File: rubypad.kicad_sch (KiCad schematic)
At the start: 1 part

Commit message: save changes
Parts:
- removed U?: Elite-C, symbol keebio:Elite-C
- added D1, D2, D3, D4, D5, D6: D_Small, Keebio-Parts:Diode-dual, symbol Device:D_Small
- added MX1, MX2, MX3, MX4, MX5, MX6: MX-NoLED, MX_Only:MXOnly-1U-Hotswap-Antishear, symbol MX_Alps_Hybrid:MX-NoLED
- added U1: ProMicro, Keebio-Parts:ArduinoProMicro, symbol keebio:ProMicro
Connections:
- new net: D6.2 (A), MX6.2 (ROW)
- new net: D1.2 (A), MX1.2 (ROW)
- new net: D5.2 (A), MX5.2 (ROW)
- new net: D3.2 (A), MX3.2 (ROW)
- new net: D4.2 (A), MX4.2 (ROW)
- new net: D2.2 (A), MX2.2 (ROW)
- new net col0: MX1.1 (COL), MX4.1 (COL)
- new net col1: MX2.1 (COL), MX5.1 (COL)
- new net col2: MX3.1 (COL), MX6.1 (COL)
- new net row0: D1.1 (K), D2.1 (K), D3.1 (K)
- new net row1: D4.1 (K), D5.1 (K), D6.1 (K)

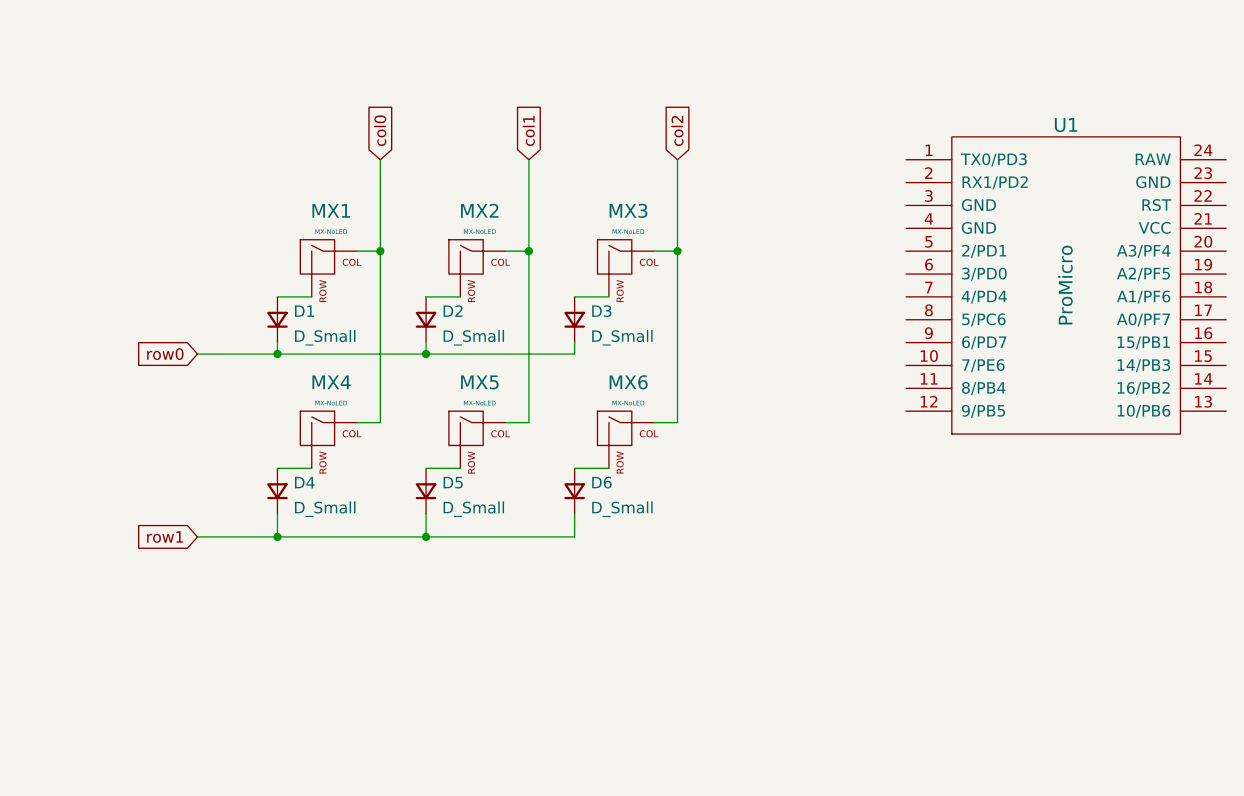
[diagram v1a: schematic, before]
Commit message: Setup encoder schematic
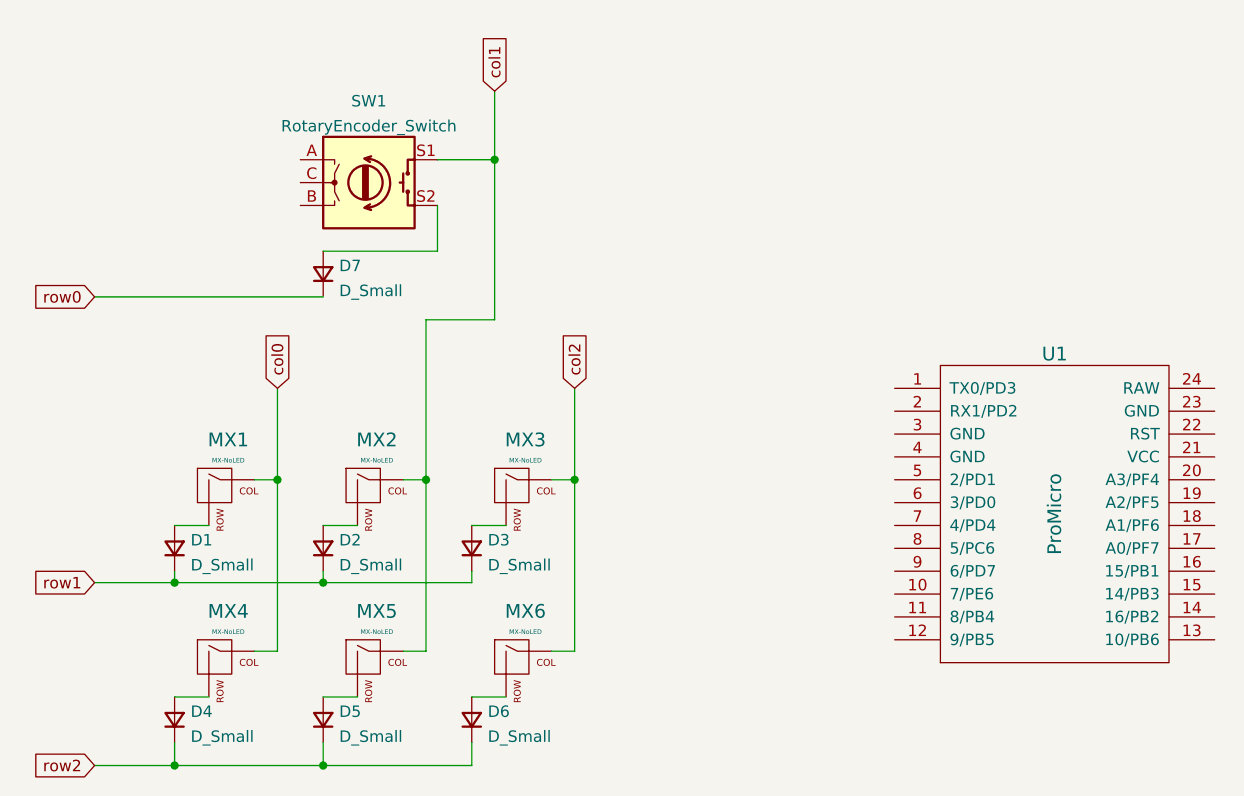
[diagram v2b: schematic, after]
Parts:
- added D7: D_Small, Keebio-Parts:Diode-dual, symbol Device:D_Small
- added SW1: RotaryEncoder_Switch, Keebio-Parts:RotaryEncoder_EC11, symbol Device:RotaryEncoder_Switch
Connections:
- net col1: now also SW1.S1
- net row0: now also D7.1 (K); no longer D1.1 (K), D2.1 (K), D3.1 (K)
- net row1: now also D1.1 (K), D2.1 (K), D3.1 (K); no longer D4.1 (K), D5.1 (K), D6.1 (K)
- new net: D7.2 (A), SW1.S2
- new net row2: D4.1 (K), D5.1 (K), D6.1 (K)
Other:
- moved on the sheet: D1, D2, D3, D4, D5, D6, MX1, MX2, MX3, MX4, MX5, MX6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

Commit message: Update - ran traces
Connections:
- net col0: now also U1.7 (4/PD4)
- net col1: now also U1.8 (5/PC6)
- net col2: now also U1.9 (6/PD7)
- net row0: now also U1.10 (7/PE6)
- net row1: now also U1.12 (9/PB5)
- net row2: now also U1.11 (8/PB4)
- net ENCB: now reaches U1.13 (10/PB6)
- net ENCB: now also SW1.B
- net ENCC: now reaches U1.14 (16/PB2)
- net ENCC: now also SW1.C
- net ENCA: now reaches U1.15 (14/PB3)
- net ENCA: now also SW1.A
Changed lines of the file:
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@@
+    (stroke (width 0) (type default) (color 0 0 0 0))
+  )
+  (wire (pts (xy 165.1 80.01) (xy 179.07 80.01))
     (stroke (width 0) (type default) (color 0 0 0 0))
   )
@@
     (stroke (width 0) (type default) (color 0 0 0 0))
   )
+  (wire (pts (xy 55.88 31.75) (xy 63.5 31.75))
+    (stroke (width 0) (type default) (color 0 0 0 0))
+  )
   (wire (pts (xy 85.09 29.21) (xy 85.09 46.99))
     (stroke (width 0) (type default) (color 0 0 0 0))
@@
     (stroke (width 0) (type default) (color 0 0 0 0))
   )
+  (wire (pts (xy 119.38 80.01) (xy 129.54 80.01))
+    (stroke (width 0) (type default) (color 0 0 0 0))
+  )
+  (wire (pts (xy 165.1 82.55) (xy 171.45 82.55))
+    (stroke (width 0) (type default) (color 0 0 0 0))
+  )
   (wire (pts (xy 74.93 64.77) (xy 77.47 64.77))
     (stroke (width 0) (type default) (color 0 0 0 0))
   )
+  (wire (pts (xy 123.19 82.55) (xy 129.54 82.55))
+    (stroke (width 0) (type default) (color 0 0 0 0))
+  )
   (wire (pts (xy 66.04 88.9) (xy 69.85 88.9))
     (stroke (width 0) (type default) (color 0 0 0 0))
@@
     )
   )
+  (global_label "ENCB" (shape input) (at 63.5 34.29 180) (fields_autoplaced)
+    (effects (font (size 1.27 1.27)) (justify right))
+    (property "Intersheet References" "${INTERSHEET_REFS}" (id 0) (at 56.0674 34.2106 0)
+      (effects (font (size 1.27 1.27)) (justify right) hide)
+    )
+  )
+  (global_label "ENCC" (shape input) (at 179.07 80.01 0) (fields_autoplaced)
+    (effects (font (size 1.27 1.27)) (justify left))
+    (property "Intersheet References" "${INTERSHEET_REFS}" (id 0) (at 186.5026 80.0894 0)
+      (effects (font (size 1.27 1.27)) (justify left) hide)
+    )
+  )
+  (global_label "col2" (shape input) (at 129.54 74.93 180) (fields_autoplaced)
+    (effects (font (size 1.27 1.27)) (justify right))
+    (property "Intersheet References" "${INTERSHEET_REFS}" (id 0) (at 123.0145 75.0094 0)
+      (effects (font (size 1.27 1.27)) (justify right) hide)
+    )
+  )
   (global_label "row1" (shape input) (at 40.64 76.2 180) (fields_autoplaced)
     (effects (font (size 1.27 1.27)) (justify right))
@@
     )
   )
+  (global_label "row2" (shape input) (at 119.38 80.01 180) (fields_autoplaced)
+    (effects (font (size 1.27 1.27)) (justify right))
+    (property "Intersheet References" "${INTERSHEET_REFS}" (id 0) (at 112.4917 79.9306 0)
+      (effects (font (size 1.27 1.27)) (justify right) hide)
+    )
+  )
   (global_label "col2" (shape input) (at 93.98 54.61 90) (fields_autoplaced)
     (effects (font (size 1.27 1.27)) (justify left))
@@
     )
   )
+  (global_label "col0" (shape input) (at 129.54 69.85 180) (fields_autoplaced)
+    (effects (font (size 1.27 1.27)) (justify right))
+    (property "Intersheet References" "${INTERSHEET_REFS}" (id 0) (at 123.0145 69.9294 0)
+      (effects (font (size 1.27 1.27)) (justify right) hide)
+    )
+  )
   (global_label "col1" (shape input) (at 85.09 21.59 90) (fields_autoplaced)
     (effects (font (size 1.27 1.27)) (justify left))
@@
     )
   )
+  (global_label "ENCC" (shape input) (at 55.88 31.75 180) (fields_autoplaced)
+    (effects (font (size 1.27 1.27)) (justify right))
+    (property "Intersheet References" "${INTERSHEET_REFS}" (id 0) (at 48.4474 31.6706 0)
+      (effects (font (size 1.27 1.27)) (justify right) hide)
+    )
+  )
+  (global_label "row0" (shape input) (at 129.54 77.47 180) (fields_autoplaced)
+    (effects (font (size 1.27 1.27)) (justify right))
+    (property "Intersheet References" "${INTERSHEET_REFS}" (id 0) (at 122.6517 77.3906 0)
+      (effects (font (size 1.27 1.27)) (justify right) hide)
+    )
+  )
+  (global_label "ENCA" (shape input) (at 165.1 77.47 0) (fields_autoplaced)
+    (effects (font (size 1.27 1.27)) (justify left))
+    (property "Intersheet References" "${INTERSHEET_REFS}" (id 0) (at 172.3512 77.5494 0)
+      (effects (font (size 1.27 1.27)) (justify left) hide)
+    )
+  )
+  (global_label "ENCA" (shape input) (at 63.5 29.21 180) (fields_autoplaced)
+    (effects (font (size 1.27 1.27)) (justify right))
+    (property "Intersheet References" "${INTERSHEET_REFS}" (id 0) (at 56.2488 29.1306 0)
+      (effects (font (size 1.27 1.27)) (justify right) hide)
+    )
+  )
+  (global_label "row1" (shape input) (at 123.19 82.55 180) (fields_autoplaced)
+    (effects (font (size 1.27 1.27)) (justify right))
+    (property "Intersheet References" "${INTERSHEET_REFS}" (id 0) (at 116.3017 82.4706 0)
+      (effects (font (size 1.27 1.27)) (justify right) hide)
+    )
+  )
   (global_label "col0" (shape input) (at 60.96 54.61 90) (fields_autoplaced)
     (effects (font (size 1.27 1.27)) (justify left))
@@
     )
   )
+  (global_label "col1" (shape input) (at 129.54 72.39 180) (fields_autoplaced)
+    (effects (font (size 1.27 1.27)) (justify right))
+    (property "Intersheet References" "${INTERSHEET_REFS}" (id 0) (at 123.0145 72.4694 0)
+      (effects (font (size 1.27 1.27)) (justify right) hide)
+    )
+  )
+  (global_label "ENCB" (shape input) (at 171.45 82.55 0) (fields_autoplaced)
+    (effects (font (size 1.27 1.27)) (justify left))
+    (property "Intersheet References" "${INTERSHEET_REFS}" (id 0) (at 178.8826 82.6294 0)
+      (effects (font (size 1.27 1.27)) (justify left) hide)
+    )
+  )

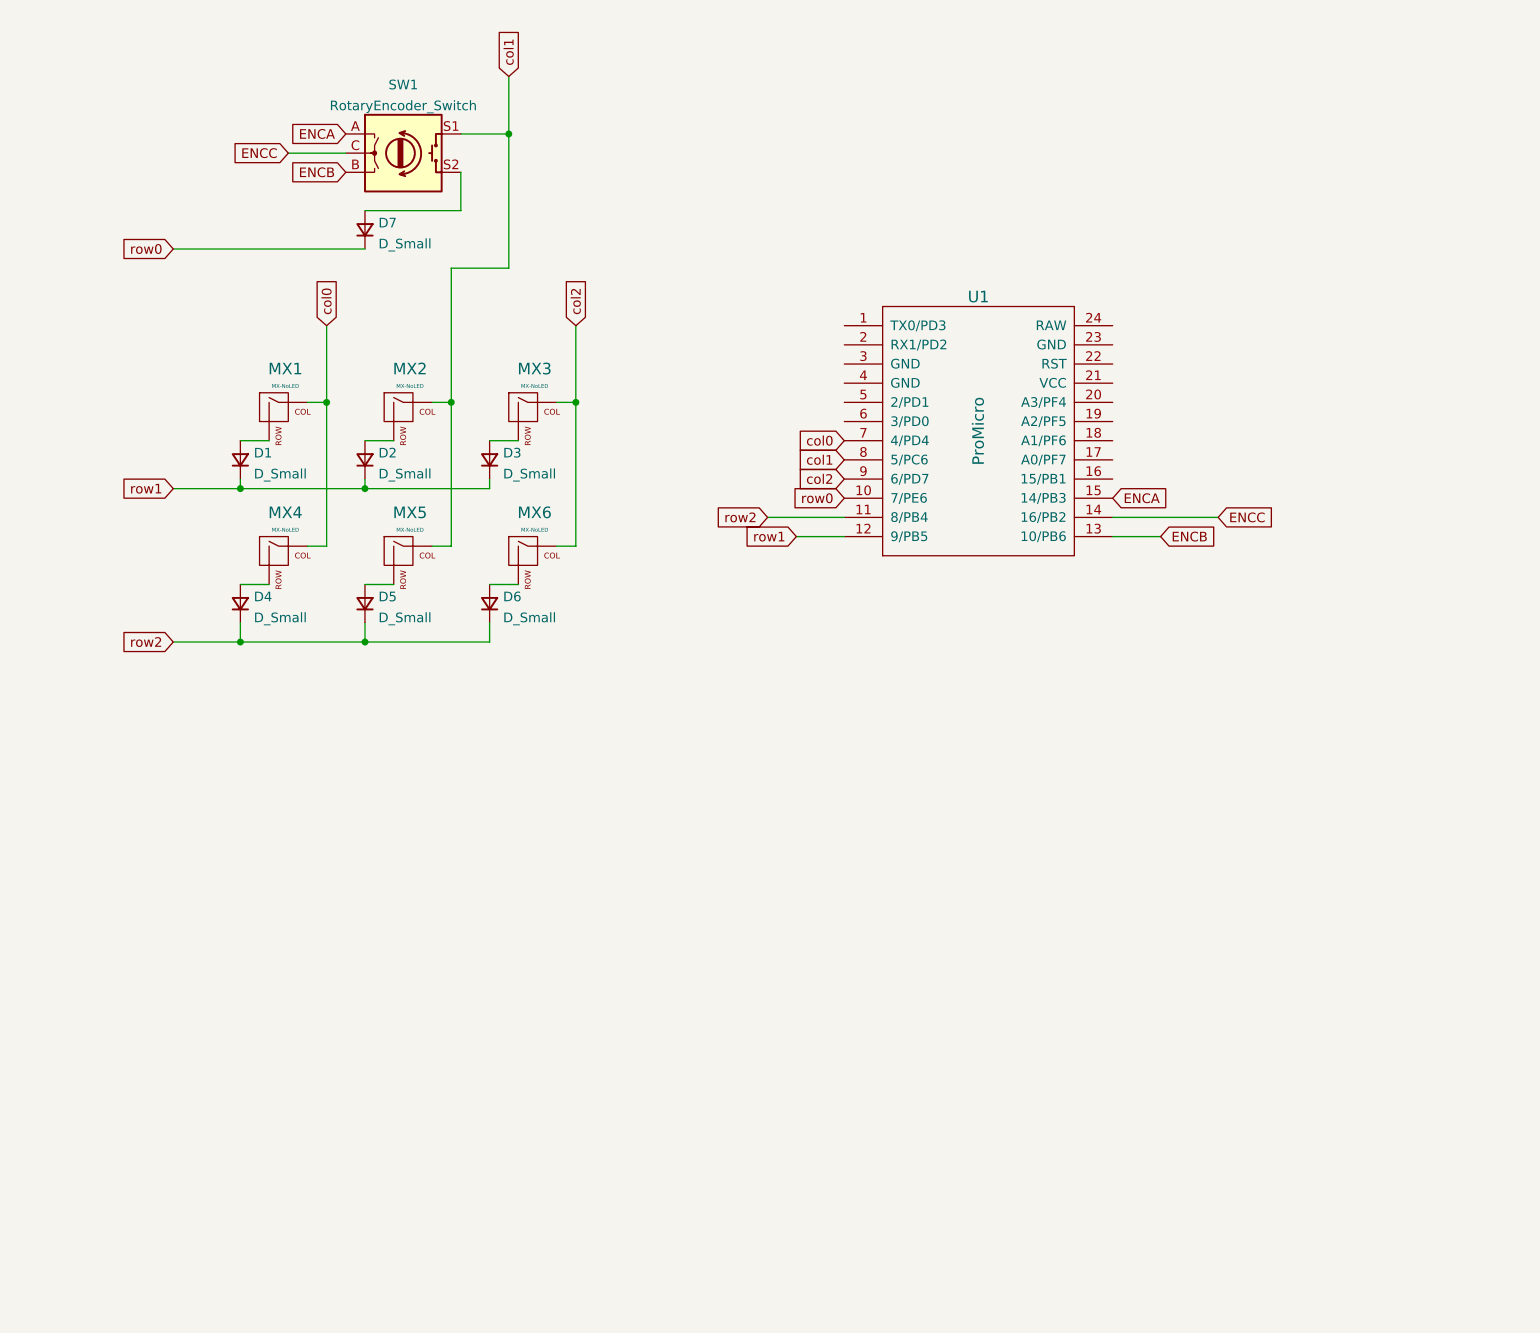
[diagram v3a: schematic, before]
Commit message: Added 3d models
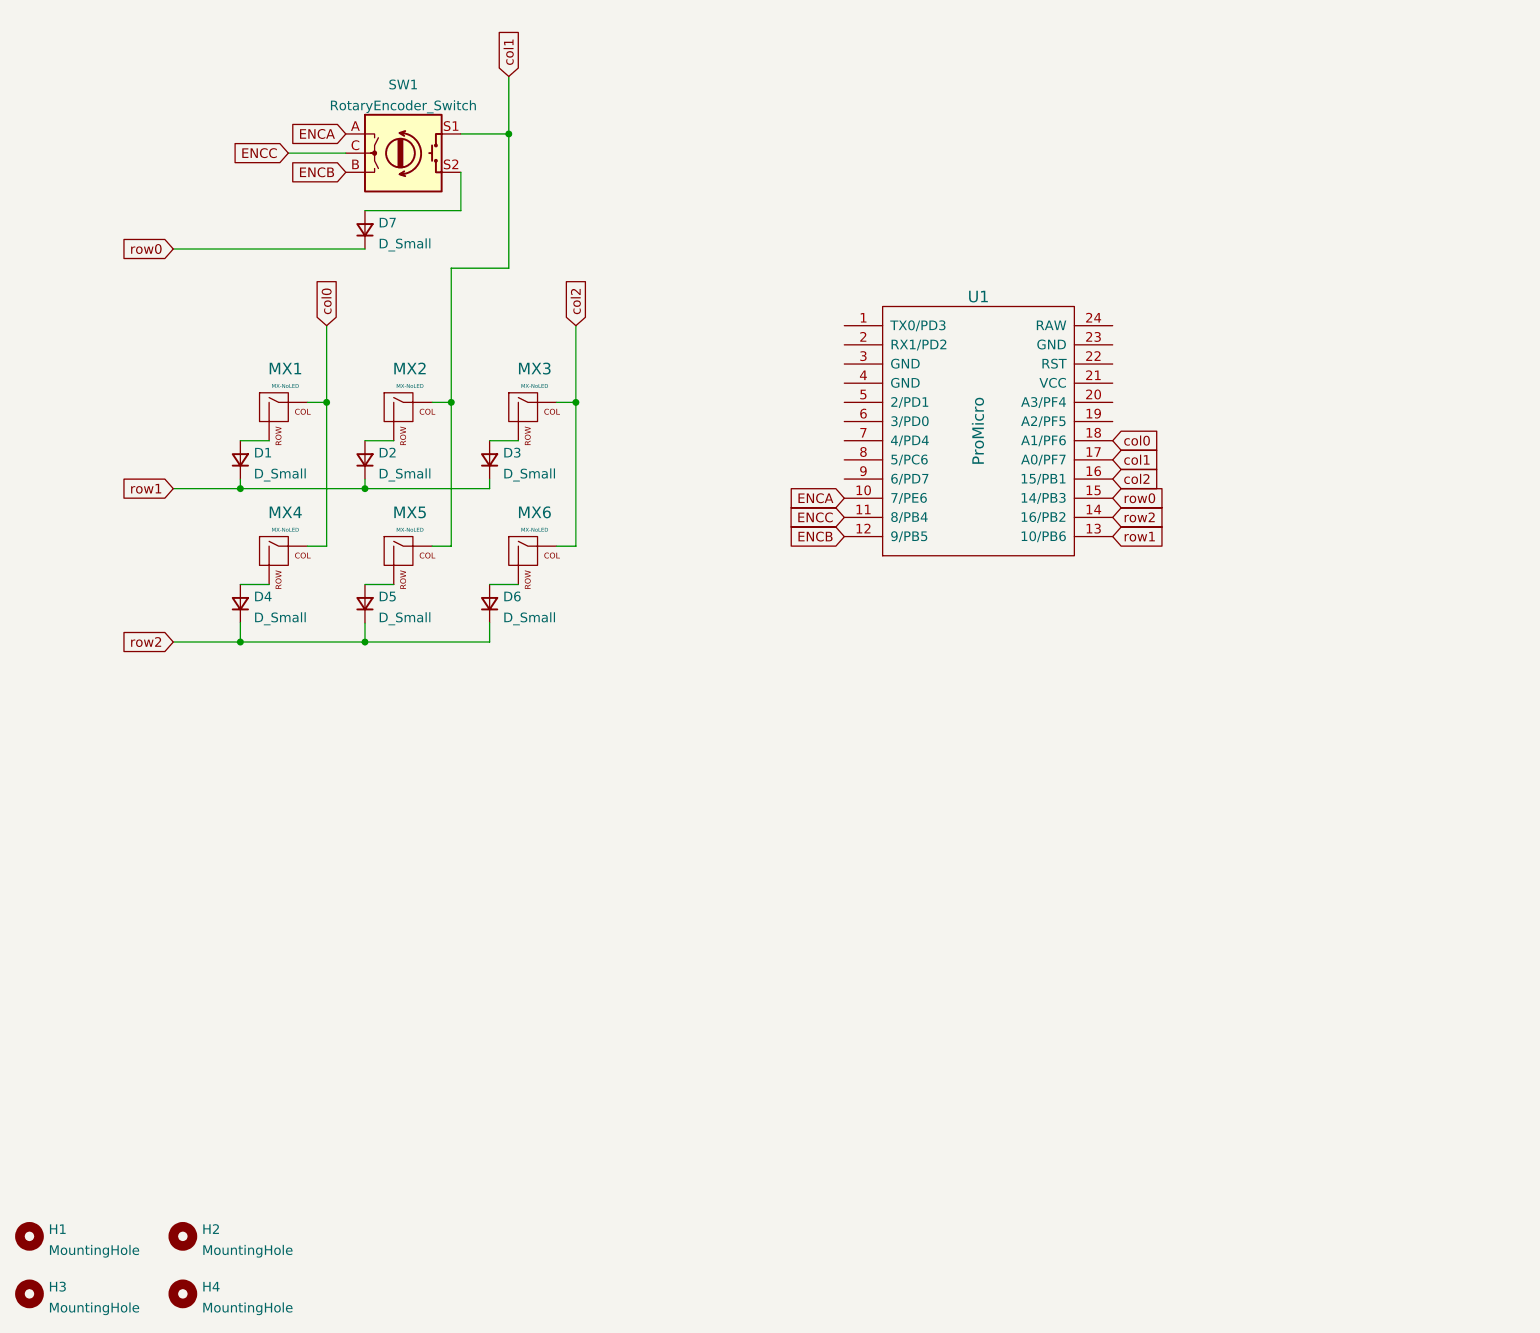
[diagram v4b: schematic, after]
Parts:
- added H1, H2, H3, H4: MountingHole, MountingHole:MountingHole_2.7mm_Pad_Via, symbol Mechanical:MountingHole
- D1, D2, D3, D4, D5, D6, D7: footprint Keebio-Parts:Diode-dual -> Diode_SMD:D_SOD-123
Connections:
- net ENCA: now also U1.10 (7/PE6); no longer U1.15 (14/PB3)
- net ENCB: now also U1.12 (9/PB5); no longer U1.13 (10/PB6)
- net ENCC: now also U1.11 (8/PB4); no longer U1.14 (16/PB2)
- net col0: now also U1.18 (A1/PF6); no longer U1.7 (4/PD4)
- net col1: now also U1.17 (A0/PF7); no longer U1.8 (5/PC6)
- net col2: now also U1.16 (15/PB1); no longer U1.9 (6/PD7)
- net row0: now also U1.15 (14/PB3); no longer U1.10 (7/PE6)
- net row1: now also U1.13 (10/PB6); no longer U1.12 (9/PB5)
- net row2: now also U1.14 (16/PB2); no longer U1.11 (8/PB4)
